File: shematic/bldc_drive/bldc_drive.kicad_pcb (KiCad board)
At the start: 2 copper layers, 106 x 65 mm, 108 parts, among them J1 Conn_01x04_Male, J2 Conn_01x04_Male, J3 Conn_01x02_Male, J4 Conn_01x02_Male, J5 Conn_01x04_Male, Q1 BC817, Q2 BC807, Q3 IRF1407, Q4 IRF1407, Q5 IRF1407, Q6 IRF1407, Q7 IRF1407, Q8 IRF1407, Q9 IRF1407, U1 24LC08, U10 TJA1051T, U11 MAX481E, U12 uA7812, U13 AP1117-33, U2 STM32F042C6Tx, U3 A1302KUA-T, U4 A1302KUA-T, U5 A1302KUA-T, U6 IR2101, U7 IR2101, U8 IR2101, U9 INA193, Y1 Crystal_GND2_Small

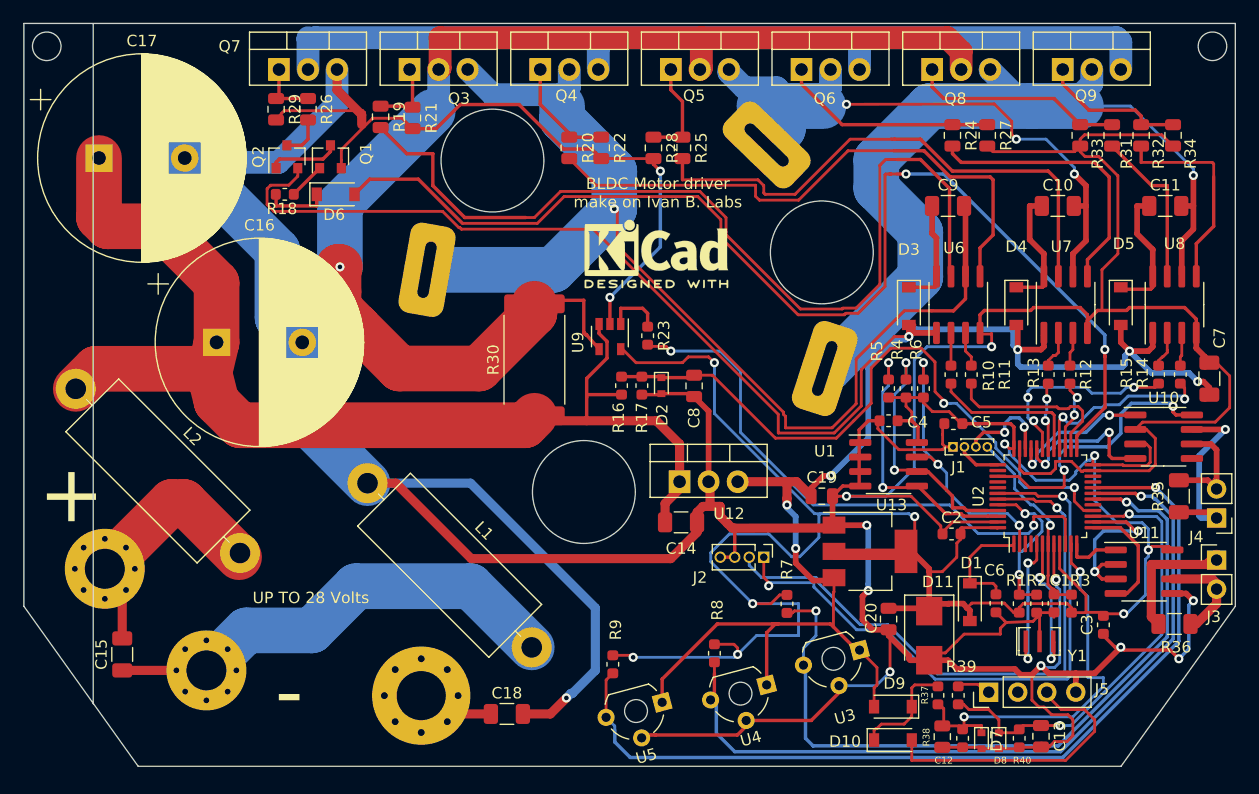
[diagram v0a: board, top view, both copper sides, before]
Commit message: modify for warios drive
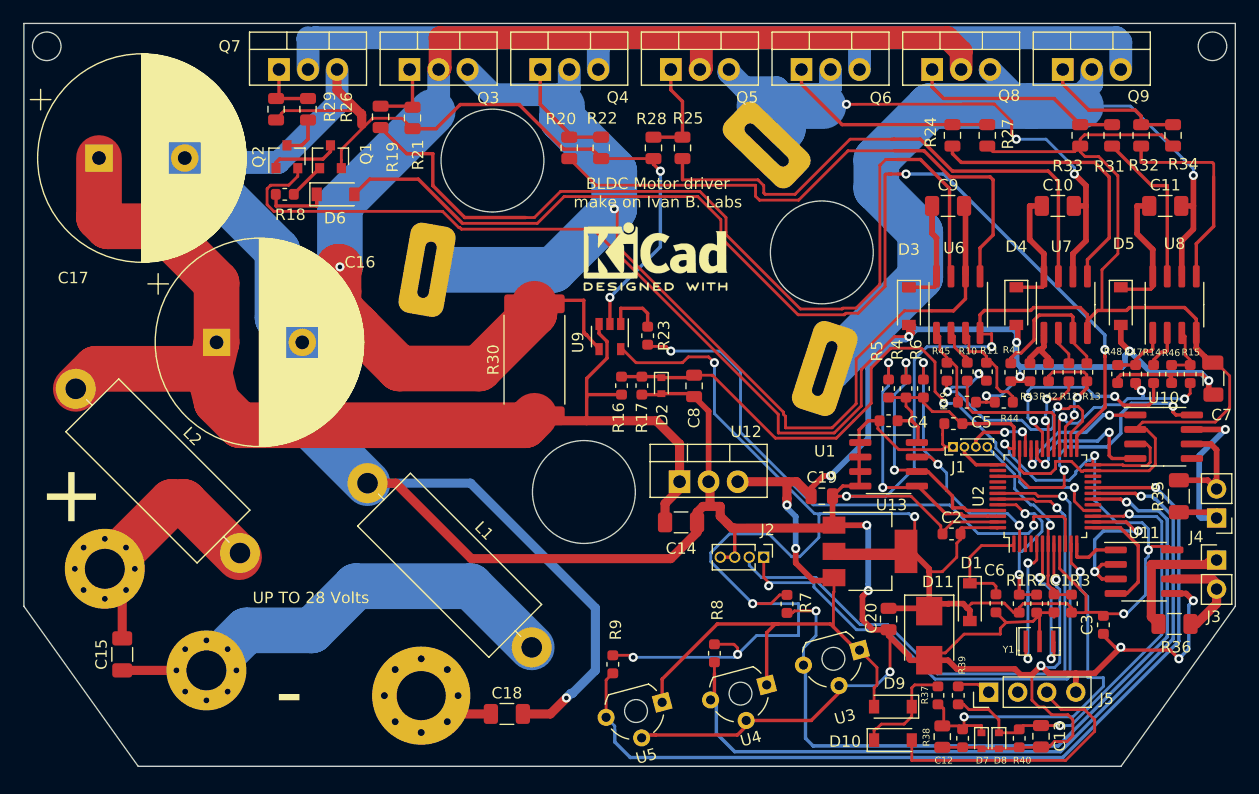
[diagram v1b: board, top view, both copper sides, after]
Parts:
- added R41: 0R**, Resistor_SMD:R_0603_1608Metric, F.Cu at (140.9, 69.7)
- added R42: 56R**, Resistor_SMD:R_0603_1608Metric, F.Cu at (144.2, 69.7)
- added R43: 0R*, Resistor_SMD:R_0603_1608Metric, F.Cu at (142.5, 69.7)
- added R44: 0R**, Resistor_SMD:R_0603_1608Metric, F.Cu at (140.3, 72.3)
- added R45: 56R**, Resistor_SMD:R_0603_1608Metric, F.Cu at (135.3, 69.6)
- added R46: 0R**, Resistor_SMD:R_0603_1608Metric, F.Cu at (154.9, 69.8)
- added R47: 56R**, Resistor_SMD:R_0603_1608Metric, F.Cu at (151.8, 69.8)
- added R48: 0R*, Resistor_SMD:R_0603_1608Metric, F.Cu at (150.2, 69.8)
- added R49: 0R*, Resistor_SMD:R_0603_1608Metric, F.Cu at (137.0, 72.3)
- R11, R13, R15: value 56R -> 56R*
- moved R12 1.81 mm to (145.9, 69.7)
- moved R13 1.49 mm to (147.5, 69.7)
- moved R10 1.44 mm to (137.1, 69.6)
- moved R11 1.35 mm to (138.7, 69.6)
- moved R15 0.87 mm to (156.6, 69.8)
- moved R14 0.43 mm to (153.4, 69.8)
- moved C7 0.36 mm to (158.6, 70.2)
- moved REF** 0.24 mm to (109.8, 59.5)
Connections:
- U6 pad 1: +12V -> Net-(R45-Pad1)
- U7 pad 1: +12V -> Net-(R42-Pad2)
- U8 pad 1: +12V -> Net-(R47-Pad1)
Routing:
- net Net-(R13-Pad1): track 3.84 -> 14.0 mm
- net LAL: track 15.4 -> 25.1 mm, vias 0 -> 3
- net +12V: track 199.6 -> 209.3 mm, vias 7 -> 9
- net Net-(R45-Pad1): track 0.00 -> 7.12 mm
- net Net-(R11-Pad1): track 3.94 -> 10.8 mm
- net Net-(R47-Pad1): track 0.00 -> 5.32 mm
- net Net-(R42-Pad2): track 0.00 -> 4.93 mm
- net LBL: track 7.48 -> 12.4 mm
- net SWDIO: track 8.63 -> 6.56 mm
- net LCL: track 16.5 -> 18.4 mm, vias 2 -> 3
- net Net-(R15-Pad1): track 3.79 -> 5.61 mm
- net LBH: track 6.16 -> 7.78 mm
- net LCH: track 17.8 -> 19.2 mm
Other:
- outline, holes or cut-outs redrawn
